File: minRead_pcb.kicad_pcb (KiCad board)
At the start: 2 copper layers, 60 x 111.3 mm, 168 parts, among them J1 USB_C_Receptacle, J2 FH34SRJ-24S-0.5SH_50_, J3 FH34SRJ-6S-0.5SH_50_, J4 FH34SRJ-6S-0.5SH_50_, J5 Conn_01x02, J6 PPPC062LJBN-RC, J7 Micro_SD_Card, Q1 FS8205A, Q12 MMBT3904, Q13 MMBT3904, Q14 AO3419, Q15 MMBT3906, Q16 MMBT3906, Q17 MMBT3904, Q2 AO3419, Q3 AO3419, Q4 BSS138, Q5 BSS138, Q6 BSS138, Q7 AO3419, Q8 AO3419, Q9 BSS138, Q9 MMBT3904, SW1 SW_Push, SW10 SW_Push, SW11 SW_Push, SW2 SW_Push, SW3 SW_Push, SW4 SW_Push, SW5 SW_Push, SW6 SW_Push, SW7 SW_Push, SW8 SW_Push, SW9 SW_Push, U1 TPD4E1U06DBVR, U10 AP3031KTR, U2 LM27313XMF, U2 TPS2116DRL, U3 AP2112K-3.3, U4 ESP32-S3-WROOM-1, U5 DW01A, U6 TPD4E1U06DBVR, U7 MCP73832-2-OT, U8 TPD4E1U06DBVR, U9 TPD4E1U06DBVR

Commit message: Schematic/PCB: finalize changes and layout progress
C- -> pin 1; W- -> pin 2; GND -> pin 3.

Schematic mostly finalized. 74 inverter used instead of PNP/NPN. ESP32 pinout configured. Components semi-optimally laid out; remaining traces TBD.
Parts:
- removed the D2 at (-57.2, 36.7)
- removed Q16: MMBT3906, Package_TO_SOT_SMD:SOT-23_Handsoldering
- removed Q17: MMBT3904, Package_TO_SOT_SMD:SOT-23_Handsoldering
- removed Q2: AO3419, Package_TO_SOT_SMD:SOT-23_Handsoldering
- removed the Q9 at (296.5, 164.7)
- removed the R38 at (-54.9, 36.7)
- removed the R39 at (291.0, 166.2)
- removed the R41 at (298.2, 160.4)
- removed R47, R48: 18k, Resistor_SMD:R_0805_2012Metric_Pad1.20x1.40mm_HandSolder
- removed the U2 at (-84.3, 38.2)
- added C29: 2.2n, Capacitor_SMD:C_0805_2012Metric_Pad1.18x1.45mm_HandSolder, B.Cu at (70.0, 88.0)
- added R62: 10k, Resistor_SMD:R_0805_2012Metric_Pad1.20x1.40mm_HandSolder, B.Cu at (103.0, 63.5)
- added R63: 100, Resistor_SMD:R_0805_2012Metric_Pad1.20x1.40mm_HandSolder, B.Cu at (111.0, 123.5)
- added R64: 100, Resistor_SMD:R_0805_2012Metric_Pad1.20x1.40mm_HandSolder, B.Cu at (111.0, 126.5)
- added R65: 33, Resistor_SMD:R_0805_2012Metric_Pad1.20x1.40mm_HandSolder, B.Cu at (36.5, 120.5)
- added U11: TP4056-42-ESOP8, Package_SO:SOIC-8-1EP_3.9x4.9mm_P1.27mm_EP2.41x3.3mm_ThermalVias, B.Cu at (93.7, 88.0)
- added U12: 74LVC1G04, Package_TO_SOT_SMD:SOT-23-5_HandSoldering, B.Cu at (47.9, 134.8)
- C2, C3: value 4.7u -> 10u
- C24: value 2.2n -> 100n
- D2: footprint LED_THT:LED_D3.0mm -> LED_SMD:LED_1206_3216Metric_Pad1.42x1.75mm_HandSolder
- R6: value 10k -> 12k
- U7: value MCP73832-2-OT -> TPD4E1U06DBVR; footprint Package_TO_SOT_SMD:SOT-23-5 -> Package_TO_SOT_SMD:SOT-23-6_Handsoldering
- moved R42 264.6 mm to (47.4, 120.9), turned to 0 degrees
- moved R39 263.1 mm to (48.5, 123.8), turned to -90 degrees
- moved R45 260.4 mm to (46.5, 123.7), turned to -90 degrees
- moved R44 257.2 mm to (55.0, 122.5)
- moved R49 256.5 mm to (50.5, 125.1), turned to 90 degrees
- moved Q9 256.0 mm to (51.1, 121.0), turned to 90 degrees
- moved R17 255.8 mm to (55.8, 119.6), turned to -90 degrees
- moved R50 255.5 mm to (51.4, 133.6), turned to -90 degrees
- moved D9 253.6 mm to (58.3, 129.7), turned to 90 degrees
- moved R43 253.4 mm to (58.8, 118.9), turned to 0 degrees
- moved R41 253.3 mm to (58.3, 133.9), turned to -90 degrees
- moved R46 253.1 mm to (53.8, 119.5), turned to 90 degrees
- moved R37 250.4 mm to (46.4, 131.1)
- moved G*** 246.1 mm to (123.8, 33.0)
- moved Q6 245.9 mm to (48.4, 127.5), turned to 0 degrees
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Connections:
- net EPD_MOSI renamed SPI_MOSI
- net EPD_SCK renamed SPI_SCK
- C24 pad 1: /COLOR_SEL_INV -> 3V3
- D8 pad 2: GND -> W-
- D8 pad 3: W- -> GND
- J4 pad 3: RST -> TP_RST
- J4 pad 4: INT -> TP_INT
- J4 pad 5: SDA -> I2C_SDA
- J4 pad 6: SCL -> I2C_SCL
- J6 pad 10: UNUSED_GPIO_16 -> unconnected-(J6-Pad10)
- J6 pad 11: TX -> unconnected-(J6-Pad11)
- J6 pad 3: UNUSED_GPIO_45 -> unconnected-(J6-Pad3)
- J6 pad 4: UNUSED_GPIO_47 -> unconnected-(J6-Pad4)
- J6 pad 5: UNUSED_GPIO_15 -> unconnected-(J6-Pad5)
- J6 pad 6: RX -> unconnected-(J6-Pad6)
- J6 pad 9: UNUSED_GPIO_46 -> unconnected-(J6-Pad9)
- Q12 pad 3: Net-(Q12-C) -> /ISO_GATE
- Q5 pad 3: C- -> W-
- Q6 pad 3: W- -> C-
- Q9 pad 1: Net-(Q12-C) -> /ISO_GATE
- R21 pad 1: Net-(U4-IO42) -> Net-(U4-IO17)
- R22 pad 1: Net-(U4-IO41) -> Net-(U4-IO16)
- R23 pad 1: Net-(U4-IO40) -> Net-(U4-IO15)
- R24 pad 1: Net-(U4-IO38) -> Net-(U4-IO6)
- R25 pad 1: Net-(U4-IO39) -> Net-(U4-IO7)
- R26 pad 1: Net-(U4-IO48) -> Net-(U4-IO5)
- R29 pad 2: Net-(U4-IO9) -> Net-(U4-IO12)
- R30 pad 2: Net-(U4-IO10) -> Net-(U4-IO13)
- R31 pad 2: Net-(U4-IO11) -> Net-(U4-IO14)
- R32 pad 2: Net-(U4-IO12) -> Net-(U4-IO21)
- R33 pad 2: Net-(U4-IO13) -> Net-(U4-IO47)
- R34 pad 2: Net-(U4-IO14) -> Net-(U4-IO48)
- R42 pad 2: Net-(Q12-C) -> /ISO_GATE
- R43 pad 2: Net-(Q12-C) -> /ISO_GATE
- R49 pad 1: W- -> C-
- R50 pad 1: C- -> W-
- R59 pad 2: Net-(U7-STAT) -> Net-(U11-~{CHRG})
- R6 pad 1: Net-(U7-PROG) -> Net-(U11-PROG)
- SW10 pad 1: PWR_BUTTON -> Net-(R62-Pad1)
- SW11 pad 2: ESP32_EN -> Net-(R63-Pad1)
- SW6 pad 2: ESP32_IO0 -> Net-(R64-Pad1)
- U1 pad 1: SD_DAT2 -> SD_DAT3
- U1 pad 3: SD_DAT1 -> SD_DAT2
- U1 pad 4: SD_DAT0 -> SD_DAT1
- U1 pad 6: SD_DAT3 -> SD_DAT0
- U4 pad 10: LED_PWR -> Net-(U4-IO17)
- U4 pad 11: unconnected-(U4-IO18-Pad11) -> PWR_BUTTON
- U4 pad 12: CHG_STATUS -> BAT_MONIT
- U4 pad 15: PWR_BUTTON -> UNUSED_GPIO_3
- U4 pad 16: UNUSED_GPIO_46 -> unconnected-(U4-IO46-Pad16)
- U4 pad 17: Net-(U4-IO9) -> USB_STAT
- U4 pad 18: Net-(U4-IO10) -> TP_INT
- U4 pad 19: Net-(U4-IO11) -> TP_RST
- U4 pad 23: unconnected-(U4-IO21-Pad23) -> Net-(U4-IO21)
- U4 pad 24: UNUSED_GPIO_47 -> Net-(U4-IO47)
- U4 pad 26: UNUSED_GPIO_45 -> unconnected-(U4-IO45-Pad26)
- U4 pad 31: Net-(U4-IO38) -> I2C_SDA
- U4 pad 32: Net-(U4-IO39) -> I2C_SCL
- U4 pad 33: Net-(U4-IO40) -> PWM_LED
- U4 pad 34: Net-(U4-IO41) -> LED_ACTIVATE
- U4 pad 35: Net-(U4-IO42) -> COLOR_SEL
- U4 pad 38: BUTTON_ADC_2 -> Net-(U4-IO2)
- U4 pad 4: BAT_MONIT -> BUTTON_ADC_2
- U4 pad 5: PWM_LED -> Net-(U4-IO5)
- U4 pad 6: WARM_TOGGLE -> Net-(U4-IO6)
- U4 pad 7: unconnected-(U4-IO7-Pad7) -> Net-(U4-IO7)
- U4 pad 8: UNUSED_GPIO_15 -> Net-(U4-IO15)
- U4 pad 9: UNUSED_GPIO_16 -> Net-(U4-IO16)
- U7 pad 1: Net-(U7-STAT) -> TP_INT
- U7 pad 3: P+ -> TP_RST
- U7 pad 4: USB_VBUS -> I2C_SDA
- U7 pad 5: Net-(U7-PROG) -> (no net)
- U8 pad 1: UNUSED_GPIO_47 -> unconnected-(U8-Pad1)
- U8 pad 3: TX -> unconnected-(U8-Pad3)
- U8 pad 6: UNUSED_GPIO_46 -> unconnected-(U8-Pad6)
- U9 pad 1: UNUSED_GPIO_45 -> SD_CLK
- U9 pad 3: UNUSED_GPIO_15 -> SD_CMD
- U9 pad 4: RX -> unconnected-(U9-Pad4)
- U9 pad 6: UNUSED_GPIO_16 -> unconnected-(U9-Pad6)
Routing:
- net 3V3: track 0.00 -> 334.1 mm, vias 0 -> 23
- net W-: track 0.00 -> 155.1 mm, vias 0 -> 1
- net C-: track 0.00 -> 151.8 mm, vias 0 -> 1
- net BUTTON_ADC_2: track 0.00 -> 129.1 mm, vias 0 -> 2
- net BUTTON_ADC_1: track 0.00 -> 100.3 mm
- net PWR_BUTTON: track 0.00 -> 74.5 mm
- net I2C_SCL: track 0.00 -> 70.4 mm
- net I2C_SDA: track 0.00 -> 67.0 mm
- net USB_VBUS: track 0.00 -> 61.7 mm, vias 0 -> 4
- net /GDR: track 0.00 -> 54.1 mm
- net /RESE: track 0.00 -> 43.7 mm
- net DP: track 0.00 -> 42.8 mm
- net TP_INT: track 0.00 -> 42.3 mm
- net TP_RST: track 0.00 -> 42.0 mm
- net Net-(Q5-S): track 0.00 -> 40.3 mm
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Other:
- board text removed: "24"
- board text removed: "ESP32-S3 WROOM"
- board text removed: "microSD if you please"

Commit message: finished layout, schematic, tbd on next steps for review
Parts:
- SW6: footprint Button_Switch_THT:SW_PUSH_6mm -> Button_Switch_THT:SW_PUSH_1P1T_6x3.5mm_H4.3_APEM_MJTP1243
- moved R65 48.3 mm to (73.0, 88.9), turned to -90 degrees
- moved SW6 43.9 mm to (79.5, 118.3)
- moved R64 41.6 mm to (70.6, 116.6), turned to 90 degrees
- moved SW11 22.5 mm to (99.3, 131.0), turned to -90 degrees
- moved R63 10.5 mm to (100.7, 125.8), turned to 90 degrees
- moved U8 2.70 mm to (90.1, 52.5), turned to -90 degrees
- moved D6 2.31 mm to (80.8, 121.8)
- moved R5 1.65 mm to (74.9, 114.8)
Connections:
- J6 pad 10: unconnected-(J6-Pad10) -> I2C_SCL
- J6 pad 11: unconnected-(J6-Pad11) -> C-
- J6 pad 12: 3V3 -> GND
- J6 pad 2: C- -> SPI_SCK
- J6 pad 3: unconnected-(J6-Pad3) -> SPI_MISO
- J6 pad 4: unconnected-(J6-Pad4) -> I2C_SDA
- J6 pad 5: unconnected-(J6-Pad5) -> LED_SW
- J6 pad 6: unconnected-(J6-Pad6) -> W-
- J6 pad 7: LED_SW -> 3V3
- J6 pad 8: W- -> SPI_MOSI
- J6 pad 9: unconnected-(J6-Pad9) -> UNUSED_GPIO_3
- U8 pad 1: unconnected-(U8-Pad1) -> SPI_MISO
- U8 pad 3: unconnected-(U8-Pad3) -> I2C_SCL
- U8 pad 4: unconnected-(U8-Pad4) -> I2C_SDA
- U8 pad 6: unconnected-(U8-Pad6) -> UNUSED_GPIO_3
- U9 pad 4: unconnected-(U9-Pad4) -> SPI_MOSI
- U9 pad 6: unconnected-(U9-Pad6) -> SPI_SCK
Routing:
- net LED_SW: track 30.8 -> 179.6 mm, vias 0 -> 1
- net I2C_SCL: track 70.4 -> 153.2 mm, vias 0 -> 4
- net I2C_SDA: track 67.0 -> 145.1 mm, vias 0 -> 4
- net SPI_SCK: track 24.1 -> 91.8 mm, vias 0 -> 2
- net SPI_MOSI: track 26.2 -> 93.4 mm, vias 0 -> 2
- net ESP32_EN: track 9.46 -> 75.8 mm, vias 0 -> 2
- net UNUSED_GPIO_3: track 0.00 -> 62.9 mm, vias 0 -> 2
- net SPI_MISO: track 0.00 -> 60.2 mm, vias 0 -> 4
- net 3V3: track 334.1 -> 390.0 mm, vias 23 -> 24
- net Net-(U4-IO2): track 0.00 -> 31.5 mm, vias 0 -> 2
- net C-: track 151.8 -> 169.9 mm
- net W-: track 155.1 -> 166.8 mm
- net Net-(R63-Pad1): track 0.00 -> 9.78 mm
- net GND: track 0.00 -> 9.04 mm, vias 13 -> 47
- net ESP32_IO0: track 3.66 -> 9.12 mm
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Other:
- outline, holes or cut-outs redrawn

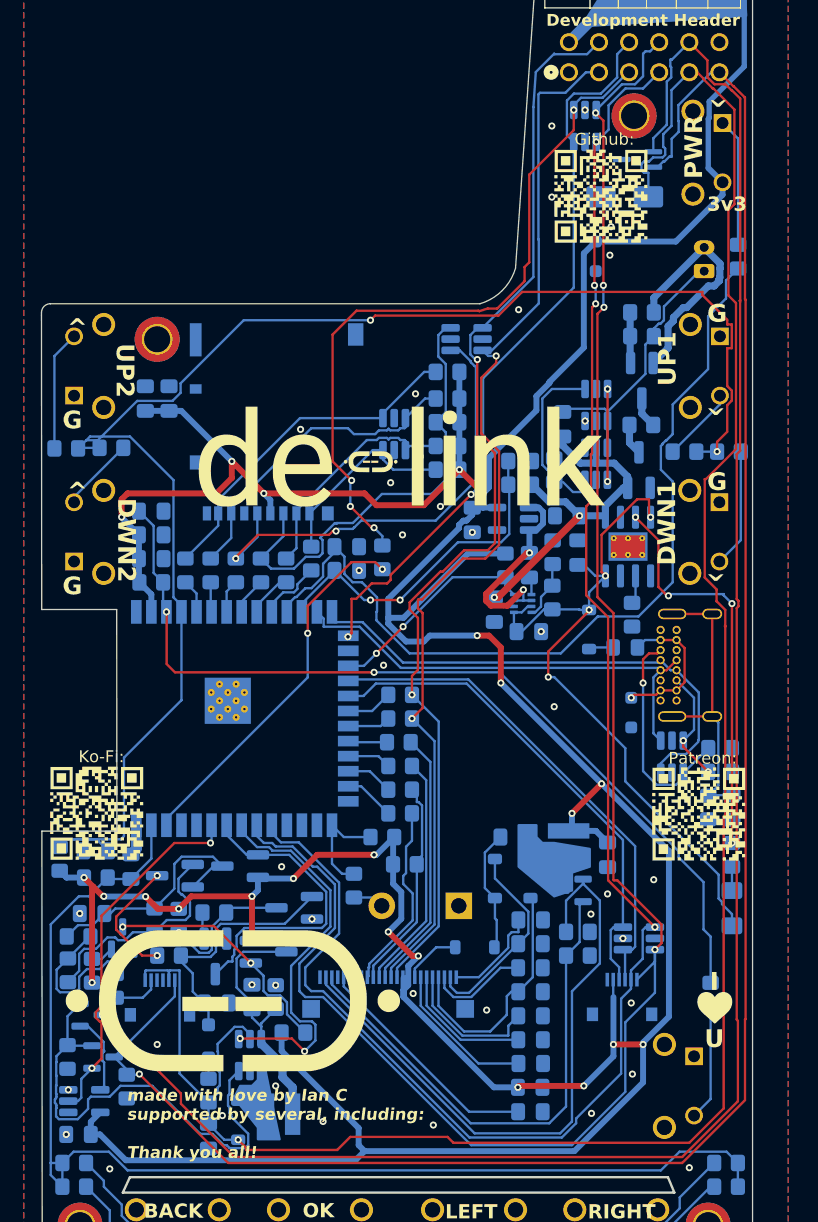
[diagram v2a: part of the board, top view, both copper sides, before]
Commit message: removed (most) vias on pads, added rtc ds3231, added TPs for UART TX/RX TBD: trace spacing, further review of habits
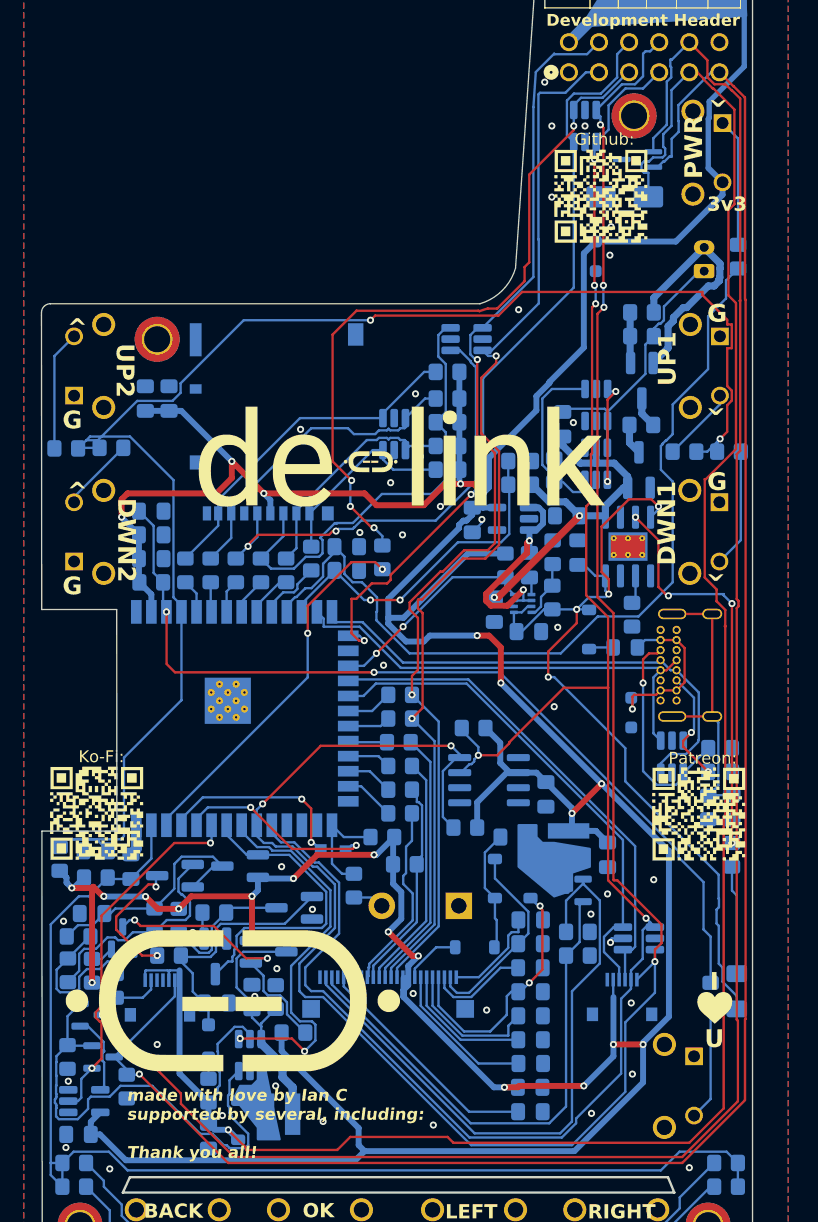
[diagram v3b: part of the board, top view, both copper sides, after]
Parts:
- added C30: 22u, Capacitor_SMD:C_0805_2012Metric_Pad1.18x1.45mm_HandSolder, B.Cu at (86.8, 108.9)
- added R47: 4.7k, Resistor_SMD:R_0805_2012Metric_Pad1.20x1.40mm_HandSolder, B.Cu at (80.0, 111.7)
- added R48: 4.7k, Resistor_SMD:R_0805_2012Metric_Pad1.20x1.40mm_HandSolder, B.Cu at (80.7, 103.3)
- added TP1: TestPoint, TestPoint:TestPoint_Pad_1.0x1.0mm, B.Cu at (69.9, 113.7)
- added TP2: TestPoint, TestPoint:TestPoint_Pad_1.0x1.0mm, B.Cu at (67.8, 113.6)
- added U13: DS3231MZ, Package_SO:SOIC-8_3.9x4.9mm_P1.27mm, B.Cu at (82.0, 107.7)
- moved D2 7.02 mm to (102.9, 125.5)
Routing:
- net I2C_SCL: track 153.2 -> 181.4 mm, vias 4 -> 6
- net 3V3: track 390.0 -> 411.3 mm
- net I2C_SDA: track 145.1 -> 163.9 mm, vias 4 -> 5
- net RX: track 0.00 -> 17.1 mm, vias 0 -> 2
- net TX: track 0.00 -> 16.6 mm, vias 0 -> 2
- net USB_VBUS: track 61.7 -> 72.8 mm
- net Net-(D2-K): track 2.01 -> 9.19 mm
- net Net-(Q7-G): track 20.5 -> 23.7 mm
- net GND: track 9.04 -> 11.8 mm, vias 47 -> 48
- net UNUSED_GPIO_3: track 62.9 -> 65.3 mm
- net /VBUS_PRE: track 12.5 -> 14.4 mm
- net SD_CLK: track 40.0 -> 38.6 mm
- net LED_SW: track 179.6 -> 180.8 mm
- net CC2: track 9.59 -> 10.6 mm
- net LDO_IN: track 17.6 -> 18.5 mm
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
